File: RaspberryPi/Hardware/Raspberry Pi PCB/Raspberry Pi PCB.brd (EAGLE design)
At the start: 80 x 60 mm, 27 parts, among them J2 1X2-3.5MM, P1 87520-0010BLF, Q11 BSS138, Q12 BSS138, U1 TPS61040QDBVRQ1, X1 0446200002

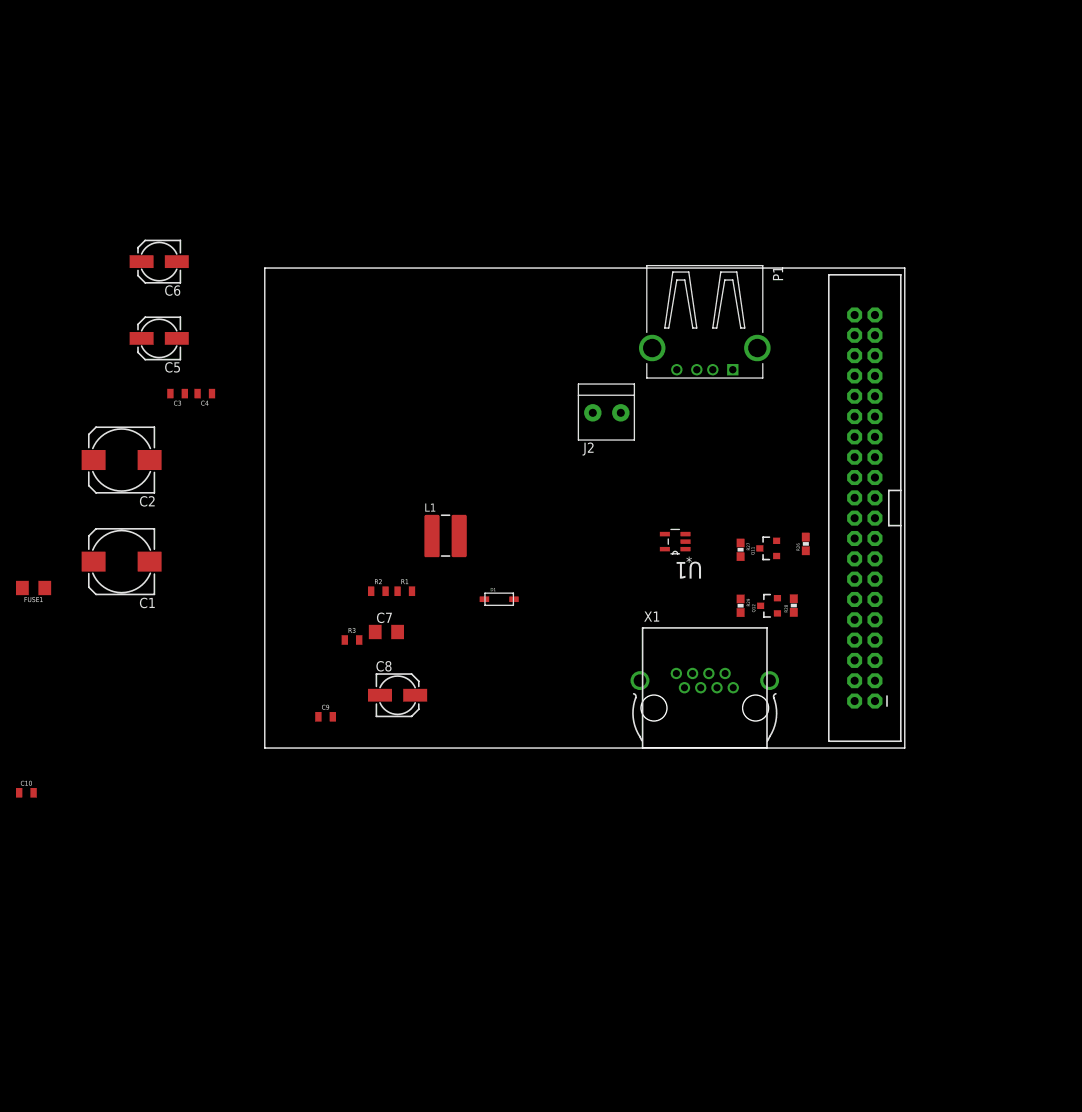
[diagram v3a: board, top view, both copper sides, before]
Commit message: Many changes to the PCB design.
Most of the required components have now been included.
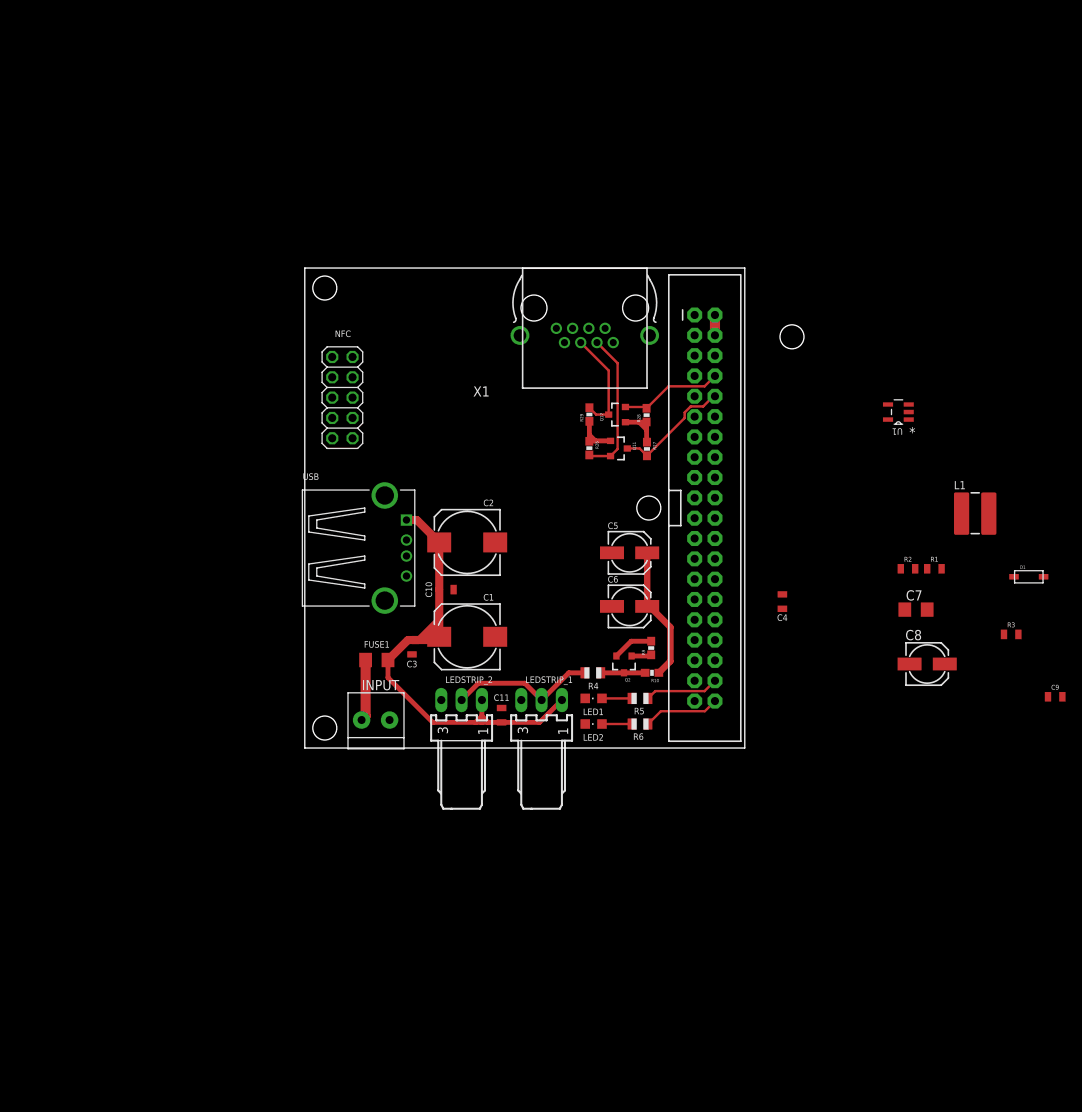
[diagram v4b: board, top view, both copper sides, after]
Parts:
- removed J2: 1X2-3.5MM, adafruit:1X2-3.5MM
- removed P1: 87520-0010BLF, 87520-0010BLF:FCI_87520-0010BLF
- added C11: 100nF, SparkFun-Capacitors:0805
- added INPUT: 1X2-3.5MM, adafruit:1X2-3.5MM
- added LED1, LED2: (no value), adafruit:CHIPLED_0805
- added LEDSTRIP_1, LEDSTRIP_2: 22-05-7038-03, con-molex:7395-03
- added NFC: (no value), pinhead:2X05
- added Q2: BSS138, SparkFun:SOT23-3
- added R10, R9: 10K, SparkFun:0603-RES
- added R4, R5, R6: (no value), adafruit:R0805
- added USB: 87520-0010BLF, 87520-0010BLF:FCI_87520-0010BLF
- JP2: value RASPBERRYPI-B+-GPIO -> RASPBERRY PI 3B
- moved C9 91.2 mm to (98.8, 6.40)
- moved R3 82.4 mm to (93.3, 14.2)
- moved C4 76.7 mm to (64.7, 18.3), turned to 270 degrees
- moved C6 72.9 mm to (45.6, 17.7), turned to 0 degrees
- moved C8 66.3 mm to (82.8, 10.5)
- moved C7 66.3 mm to (81.4, 17.3)
- moved D1 66.3 mm to (95.5, 21.4)
- moved R1 66.3 mm to (83.7, 22.4)
- moved R2 66.3 mm to (80.4, 22.4)
- moved L1 66.3 mm to (88.8, 29.3)
- moved C5 64.6 mm to (45.6, 24.4), turned to 0 degrees
- moved C10 58.3 mm to (22.7, 19.8)
- moved X1 52.2 mm to (40.0, 55.0), turned to 180 degrees
- moved C2 44.4 mm to (25.3, 25.7)
- moved C1 44.2 mm to (25.3, 13.9)
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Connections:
- removed net +5V: C1.+, C2.+, C3.1, C4.1, C5.+, C6.+, FUSE1.2, L1.1, U1.4, U1.5
- removed net GP18: JP2.12
- removed net GP20: JP2.38
- removed net GP21: JP2.40
- new net 5V_USB: C1.+, C10.1, C11.1, C2.+, C3.1, FUSE1.2, L1.1, LEDSTRIP_1.1, LEDSTRIP_2.1, U1.4, U1.5, USB.1
- new net IRQ: NFC.8
- new net LED_1: JP2.38, R5.1
- new net LED_2: JP2.40, R6.1
- new net N$3: Q2.3, R10.2, R4.1
- new net N$4: LED2.A, R6.2
- new net N$5: LED1.A, R5.2
- new net RSTOUT_N: NFC.10
- new net RSTPD_N: NFC.9
- new net SPI_CS: JP2.24, NFC.7
- new net SPI_MISO: JP2.21, NFC.5
- new net SPI_MOSI: JP2.19, NFC.6
- new net SPI_SCK: JP2.23, NFC.4
- new net VCC: X1.8
- new net WS2811_DATA_3.3V: JP2.12, Q2.2, R9.2
- new net WS2811_DATA_5V: LEDSTRIP_1.2, LEDSTRIP_2.2, R4.2
- net 3.3V: now also NFC.3, Q2.1, R9.1
- net 5V: now also C4.1, C5.+, C6.+, R10.1; no longer C10.1, P1.1
- net GND: now also C11.2, INPUT.1, LED1.C, LED2.C, LEDSTRIP_1.3, LEDSTRIP_2.3, NFC.1, NFC.2, USB.4; no longer J2.1, P1.4
- net VIN1: now also INPUT.2; no longer J2.2
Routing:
- net 5V_USB: track 0.00 -> 70.2 mm
- net 5V: track 0.00 -> 19.5 mm
- net WS2811_DATA_5V: track 0.00 -> 18.5 mm
- net TX_ATXMEGA: track 0.00 -> 18.3 mm
- net RX_RASPI: track 0.00 -> 14.8 mm
- net RX_ATXMEGA: track 0.00 -> 13.2 mm
- net TX_RASPI: track 0.00 -> 12.9 mm
- net LED_2: track 0.00 -> 9.56 mm
- net LED_1: track 0.00 -> 9.29 mm
- net 3.3V: track 0.00 -> 9.03 mm
- net VIN1: track 0.00 -> 7.71 mm
- net +12V: track 0.00 -> 6.16 mm
- net N$3: track 0.00 -> 5.55 mm
- net WS2811_DATA_3.3V: track 0.00 -> 5.12 mm
- net N$5: track 0.00 -> 3.75 mm
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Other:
- board size 80 x 60 mm -> 55 x 60 mm

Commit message: Removed the step up converter.
After some testing I found out that the voltage that is provided by the control PCB would be sufficient for the level conversion. This means that no boost converter is required.
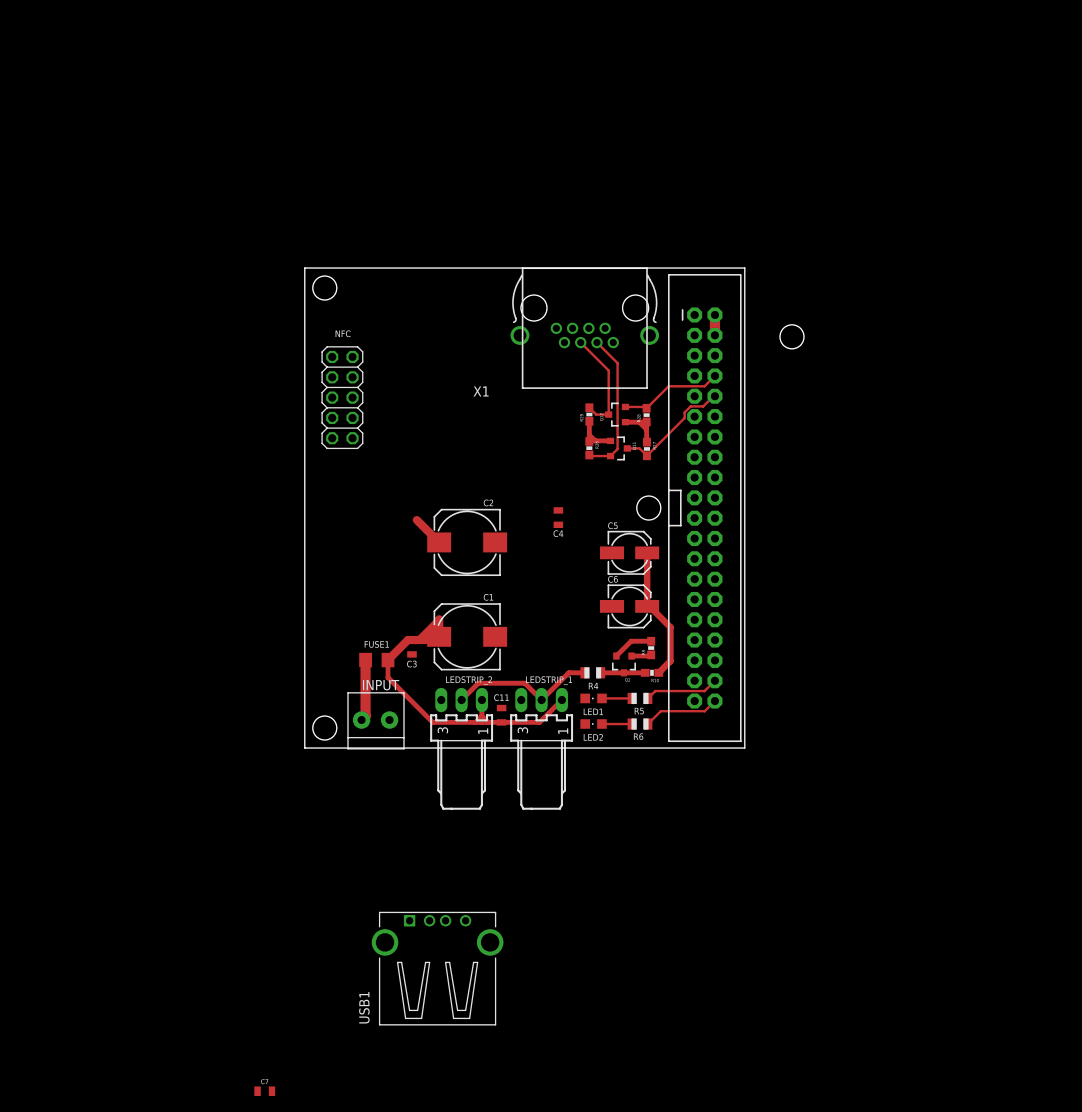
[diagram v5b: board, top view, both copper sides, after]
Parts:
- removed C10, C9: 100nF, SparkFun-Capacitors:0805
- removed C8: 10uF, adafruit:153CLV-0505
- removed D1: (no value), adafruit:SOD-123
- removed L1: CDRH4D18, inductor-sumida:CDRH4D18
- removed R1, R2, R3: (no value), SparkFun-Resistors:0805
- removed U1: TPS61040QDBVRQ1, Texas Instruments_By_element14_Batch_1:SOT95P280X145-5N
- removed USB: 87520-0010BLF, 87520-0010BLF:FCI_87520-0010BLF
- added USB1: 87520-0010BLF, 87520-0010BLF:FCI_87520-0010BLF
- C7: value (none) -> 100nF; device adafruit:C1206 -> SparkFun-Capacitors:0805
- moved C7 101.2 mm to (0.00, -42.9)
- moved C4 29.9 mm to (36.7, 28.8)
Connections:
- removed net FEEDBACK: C7.2, R1.1, R2.2, U1.3
- removed net N$1: D1.A, L1.2, U1.1
- removed net N$2: R2.1, R3.2
- net +12V: no longer C7.1, C8.+, C9.1, D1.C, R1.2
- net 5V_USB: now also C7.1, USB1.1; no longer C10.1, L1.1, U1.4, U1.5, USB.1
- net GND: now also C7.2, USB1.4; no longer C10.2, C8.-, C9.2, R3.1, U1.2, USB.4
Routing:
- net 5V_USB: track 70.2 -> 59.3 mm

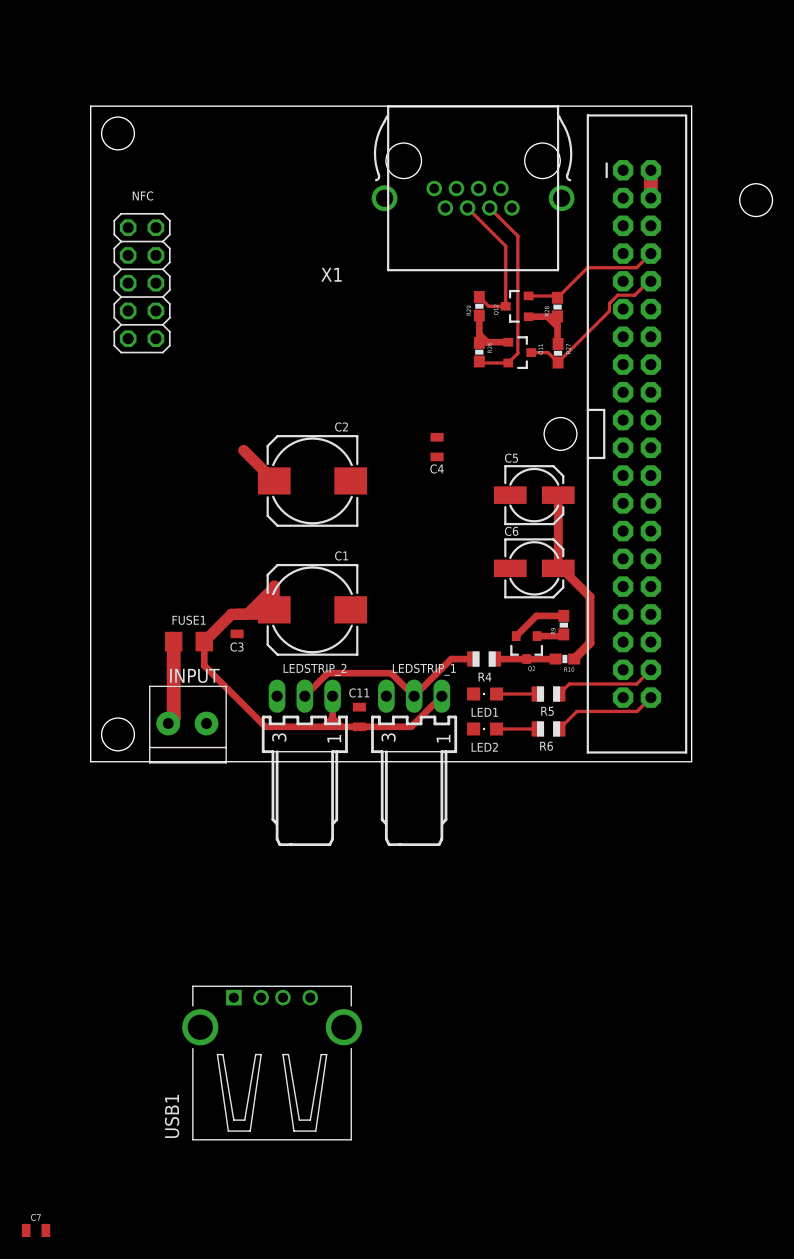
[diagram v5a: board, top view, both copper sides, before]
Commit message: Added a connector for the reed switch.
The reed switch is used to detect if the door is open. It works in combination with a magnet that is placed on the case itself.
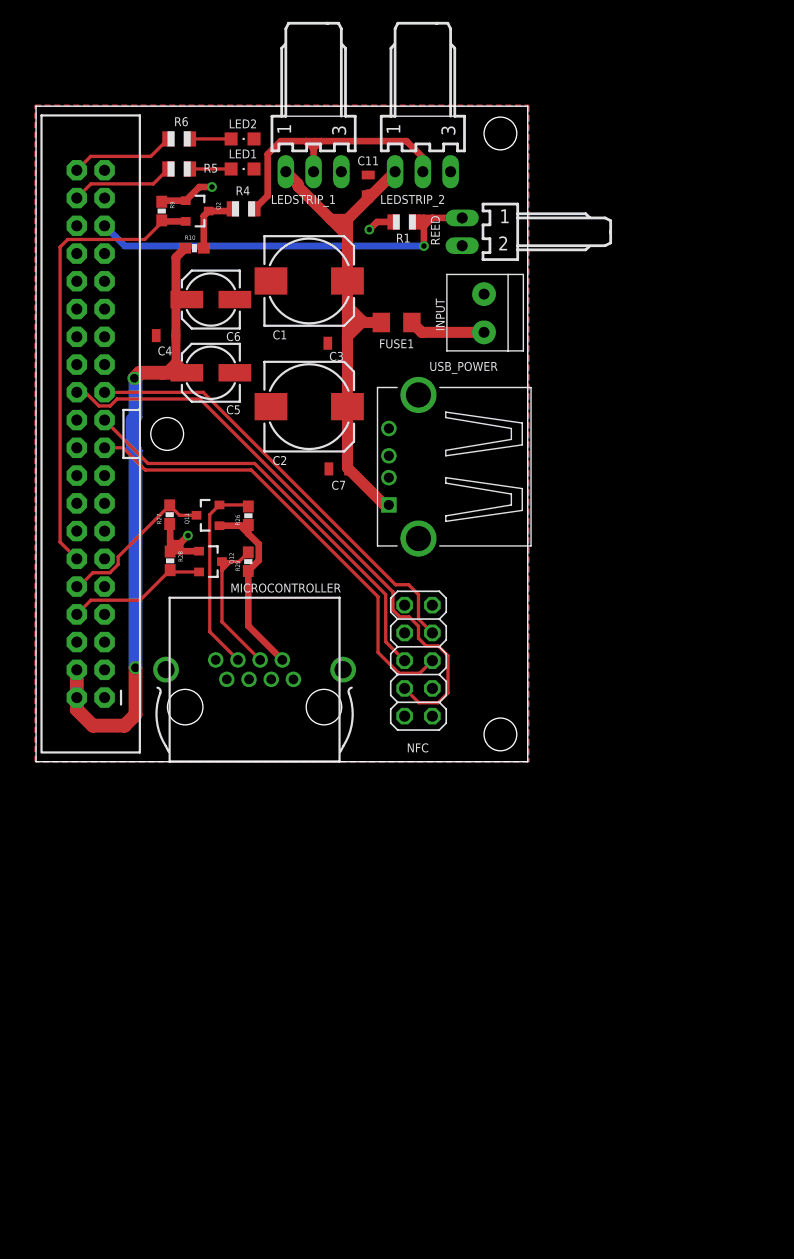
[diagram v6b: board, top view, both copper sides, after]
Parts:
- removed USB1: 87520-0010BLF, 87520-0010BLF:FCI_87520-0010BLF
- removed X1: 0446200002, con-molex:0446200002
- added MICROCONTROLLER: 0446200002, con-molex:0446200002
- added R1: (no value), adafruit:R0805
- added REED: 22-05-7028-02, con-molex:7395-02
- added USB_POWER: 87520-0010BLF, 87520-0010BLF:FCI_87520-0010BLF
- moved C7 75.0 mm to (27.7, 26.8), turned to 180 degrees
- moved R6 63.7 mm to (13.1, 57.0), turned to 0 degrees
- moved R5 58.7 mm to (13.1, 54.2), turned to 0 degrees
- moved LED2 58.4 mm to (18.9, 57.0), turned to 270 degrees
- moved LED1 52.9 mm to (18.9, 54.2), turned to 270 degrees
- moved R9 52.8 mm to (11.5, 50.4), turned to 270 degrees
- moved R10 50.6 mm to (14.5, 47.0), turned to 0 degrees
- moved Q2 50.0 mm to (14.7, 50.4), turned to 270 degrees
- moved JP2 50.0 mm to (5.00, 30.0), turned to 180 degrees
- moved LEDSTRIP_2 49.2 mm to (35.4, 54.0), turned to 180 degrees
- moved LEDSTRIP_1 48.9 mm to (25.4, 54.0), turned to 180 degrees
- moved C11 48.7 mm to (30.4, 52.8)
- moved R4 46.7 mm to (19.0, 50.6), turned to 0 degrees
- moved INPUT 46.3 mm to (41.0, 41.0), turned to 90 degrees
- moved NFC 42.8 mm to (35.0, 9.25), turned to 270 degrees
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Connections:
- removed net GP19: JP2.35
- new net REED_SWITCH: JP2.35, R1.1, REED.1
- net +12V: now also MICROCONTROLLER.2; no longer X1.2
- net 3.3V: now also R1.2
- net 5V_USB: now also USB_POWER.1; no longer USB1.1
- net GND: now also MICROCONTROLLER.1, MICROCONTROLLER.3, MICROCONTROLLER.5, MICROCONTROLLER.7, MICROCONTROLLER.S@1, MICROCONTROLLER.S@2, REED.2, USB_POWER.4; no longer USB1.4, X1.1, X1.3, X1.5, X1.7, X1.S@1, X1.S@2
- net RX_ATXMEGA: now also MICROCONTROLLER.4; no longer X1.4
- net TX_ATXMEGA: now also MICROCONTROLLER.6; no longer X1.6
- net VCC: now also MICROCONTROLLER.8; no longer X1.8
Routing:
- net SPI_CS: track 0.00 -> 54.4 mm
- net SPI_MOSI: track 0.00 -> 42.0 mm
- net 5V: track 19.5 -> 61.0 mm, vias 0 -> 2
- net SPI_SCK: track 0.00 -> 40.4 mm
- net SPI_MISO: track 0.00 -> 39.1 mm
- net REED_SWITCH: track 0.00 -> 38.1 mm, vias 0 -> 1
- net WS2811_DATA_3.3V: track 5.12 -> 41.8 mm
- net +12V: track 6.16 -> 18.1 mm
- net 3.3V: track 9.03 -> 17.9 mm, vias 0 -> 3
- net WS2811_DATA_5V: track 18.5 -> 26.9 mm
- net 5V_USB: track 59.3 -> 52.5 mm
- net RX_ATXMEGA: track 13.2 -> 15.1 mm
- net VIN1: track 7.71 -> 6.97 mm
- added copper zone on layer 16, net 3.3V
- added copper zone on layer 1, net GND
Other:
- board size 55 x 60 mm -> 45 x 60 mm
